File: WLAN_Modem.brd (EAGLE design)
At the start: 53 x 35 mm, 36 parts, among them IC1 MAX3232CSE, IC2 REG1117, J1 618009231221, J3 629722000214

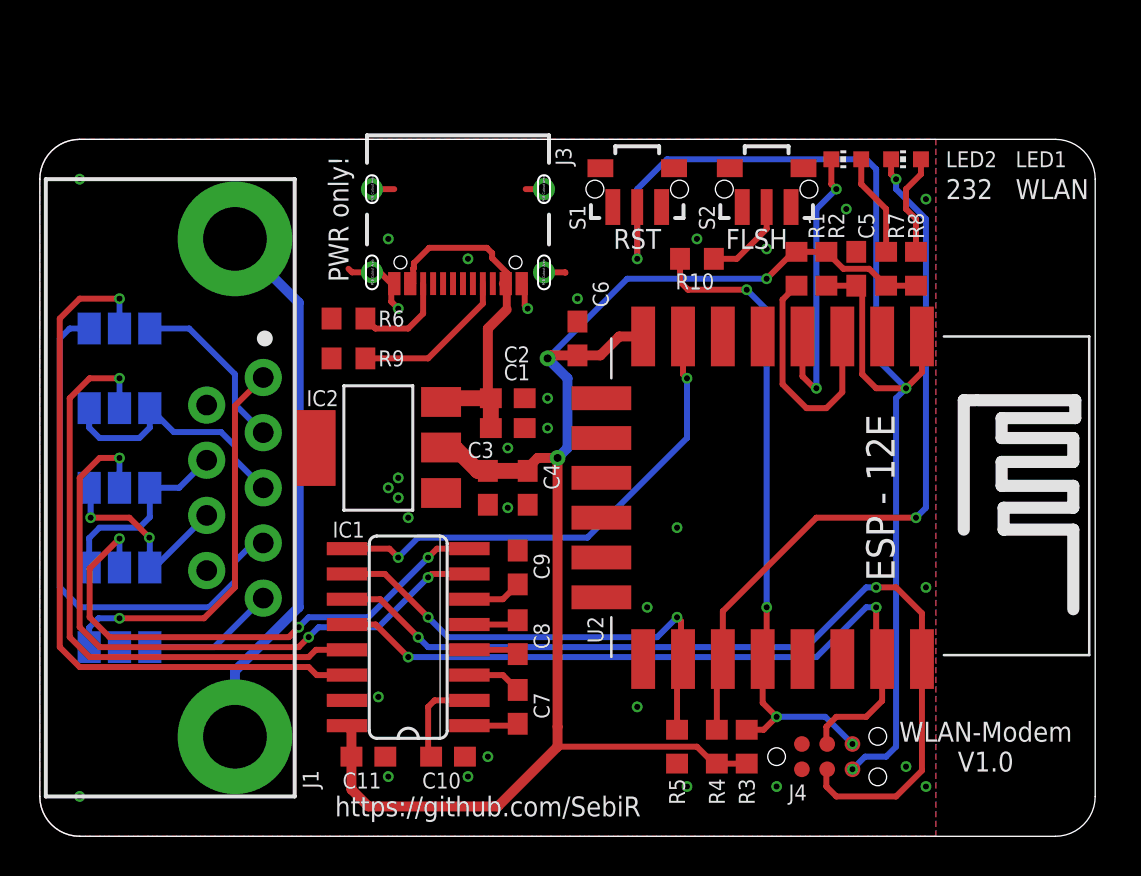
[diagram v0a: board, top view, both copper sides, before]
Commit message: * Optimized layout for manufacturing * Added plated slot note on dimension layer * Updated README.md * Added GERBER files
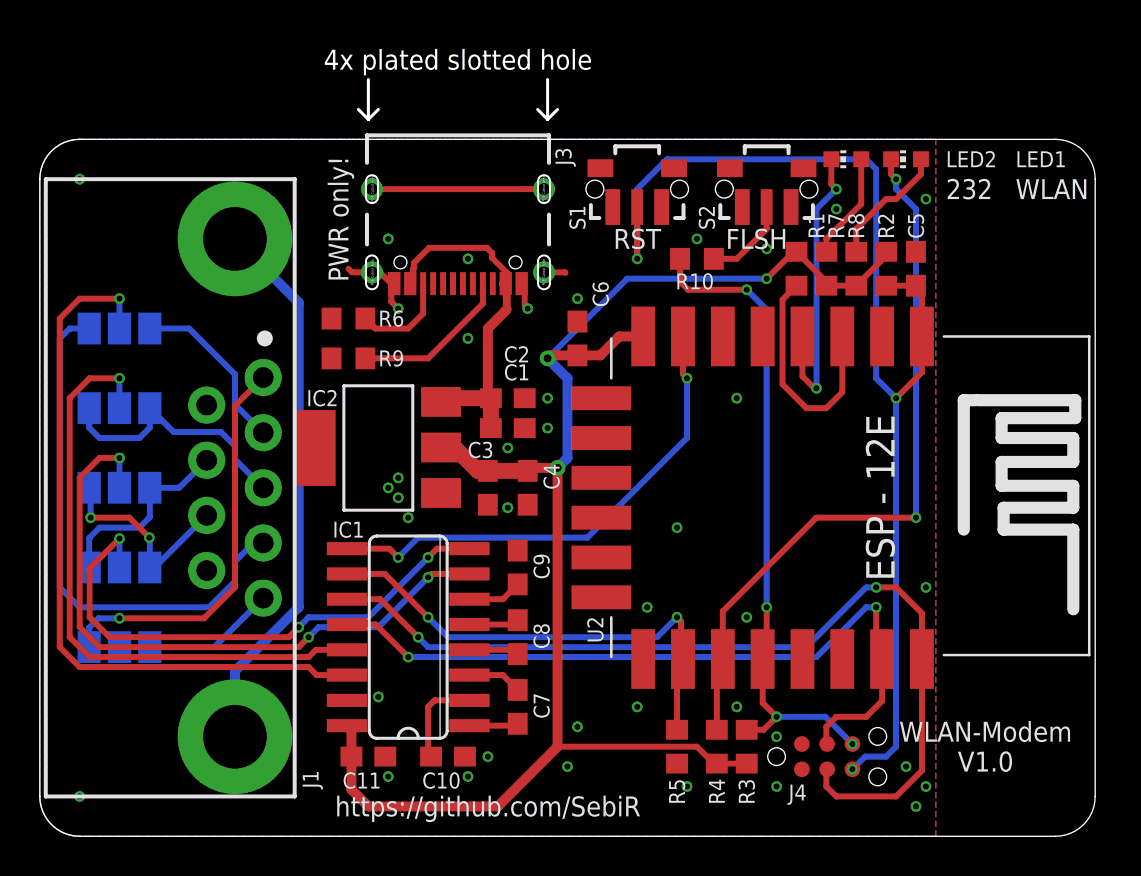
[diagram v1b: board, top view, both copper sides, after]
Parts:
- moved C5 3.00 mm to (44.0, 28.5)
- moved R2 3.00 mm to (42.5, 28.5)
- moved R7 3.00 mm to (39.5, 28.5)
- moved R8 3.00 mm to (41.0, 28.5)
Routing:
- net GND: track 36.0 -> 42.5 mm, vias 31 -> 39
- net RST: track 62.9 -> 58.8 mm
- net N$1: track 5.17 -> 6.29 mm
- net +3V3: track 78.6 -> 77.8 mm
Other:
- board size 53 x 35 mm -> 53 x 38 mm
- board text added: "4x plated slotted hole"
